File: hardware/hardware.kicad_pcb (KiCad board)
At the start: 2 copper layers, 92 x 51 mm, 44 parts, among them J1 Conn_01x06, J10 Conn_02x08_Counter_Clockwise, J11 Conn_02x08_Counter_Clockwise, J3 Conn_01x03, J4 USB_C_Receptacle_USB2.0_14P, J5 Conn_01x03, J6 RJ45, J7 RJ45, J8 Conn_02x08_Counter_Clockwise, J9 Conn_02x08_Counter_Clockwise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

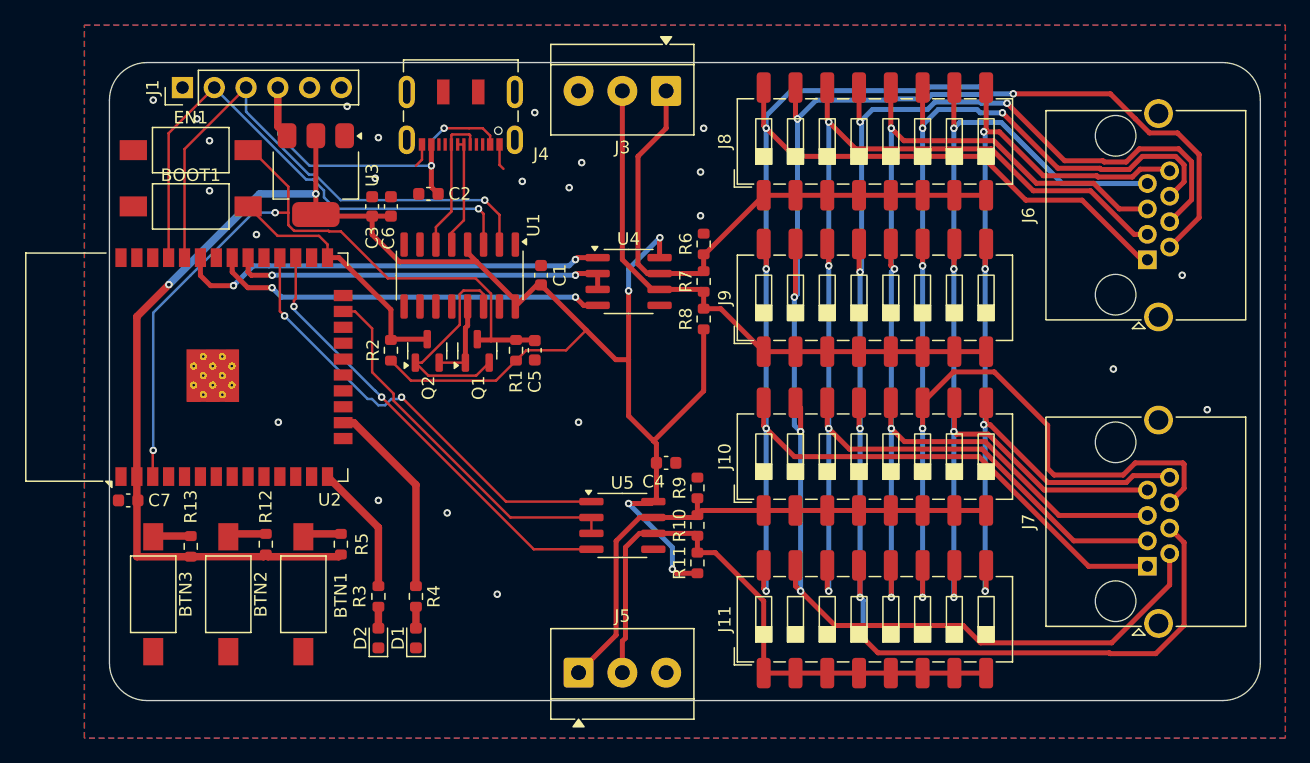
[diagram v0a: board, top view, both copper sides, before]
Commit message: rotation of ethernet connector
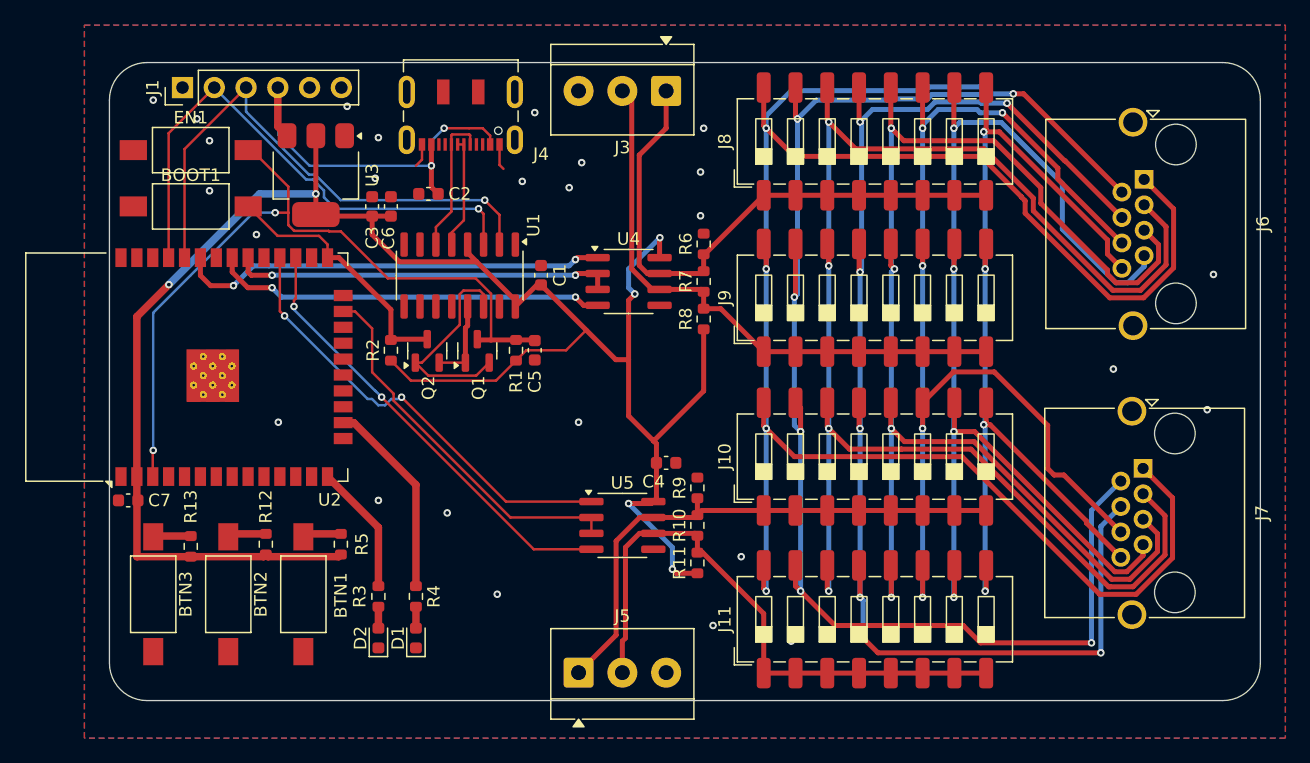
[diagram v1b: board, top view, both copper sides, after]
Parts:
- moved J7 7.83 mm to (164.6, 70.4), turned to -90 degrees
- moved J6 6.43 mm to (164.7, 47.3), turned to -90 degrees
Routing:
- net ETH1: track 136.4 -> 161.6 mm
- net ETH3: track 104.7 -> 124.6 mm
- net ETH5: track 94.2 -> 109.1 mm
- net ETH4: track 122.1 -> 108.5 mm, vias 6 -> 7
- net ETH6: track 107.0 -> 94.1 mm
- net ETH7: track 84.0 -> 94.8 mm
- net ETH2: track 128.6 -> 118.5 mm, vias 5 -> 6
- net ETH8: track 80.3 -> 78.2 mm
- net RS485_A2: track 48.2 -> 47.6 mm
- net GND: vias 23 -> 26

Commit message: add readme + pictures
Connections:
- U2 pad 10: unconnected-(U2-IO25-Pad10) -> BTN3
- U2 pad 36: unconnected-(U2-IO22-Pad36) -> BTN1
- U2 pad 37: unconnected-(U2-IO23-Pad37) -> BTN2
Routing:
- net BTN1: track 3.10 -> 36.7 mm, vias 0 -> 2
- net BTN2: track 3.10 -> 32.9 mm, vias 0 -> 2
- net BTN3: track 3.02 -> 11.5 mm
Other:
- board text added: "A1"
- board text added: "A2"
- board text added: "B1"
- board text added: "B2"
- board text added: "GND A B"
